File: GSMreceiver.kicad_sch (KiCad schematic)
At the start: 37 parts, among them J1 Conn_01x06_Pin, J2 Conn_02x02_2.54, SW1 SM5-180UP-1, U1 STM32L052C8Tx, Y1 4 MHz, Y2 32768 kHz

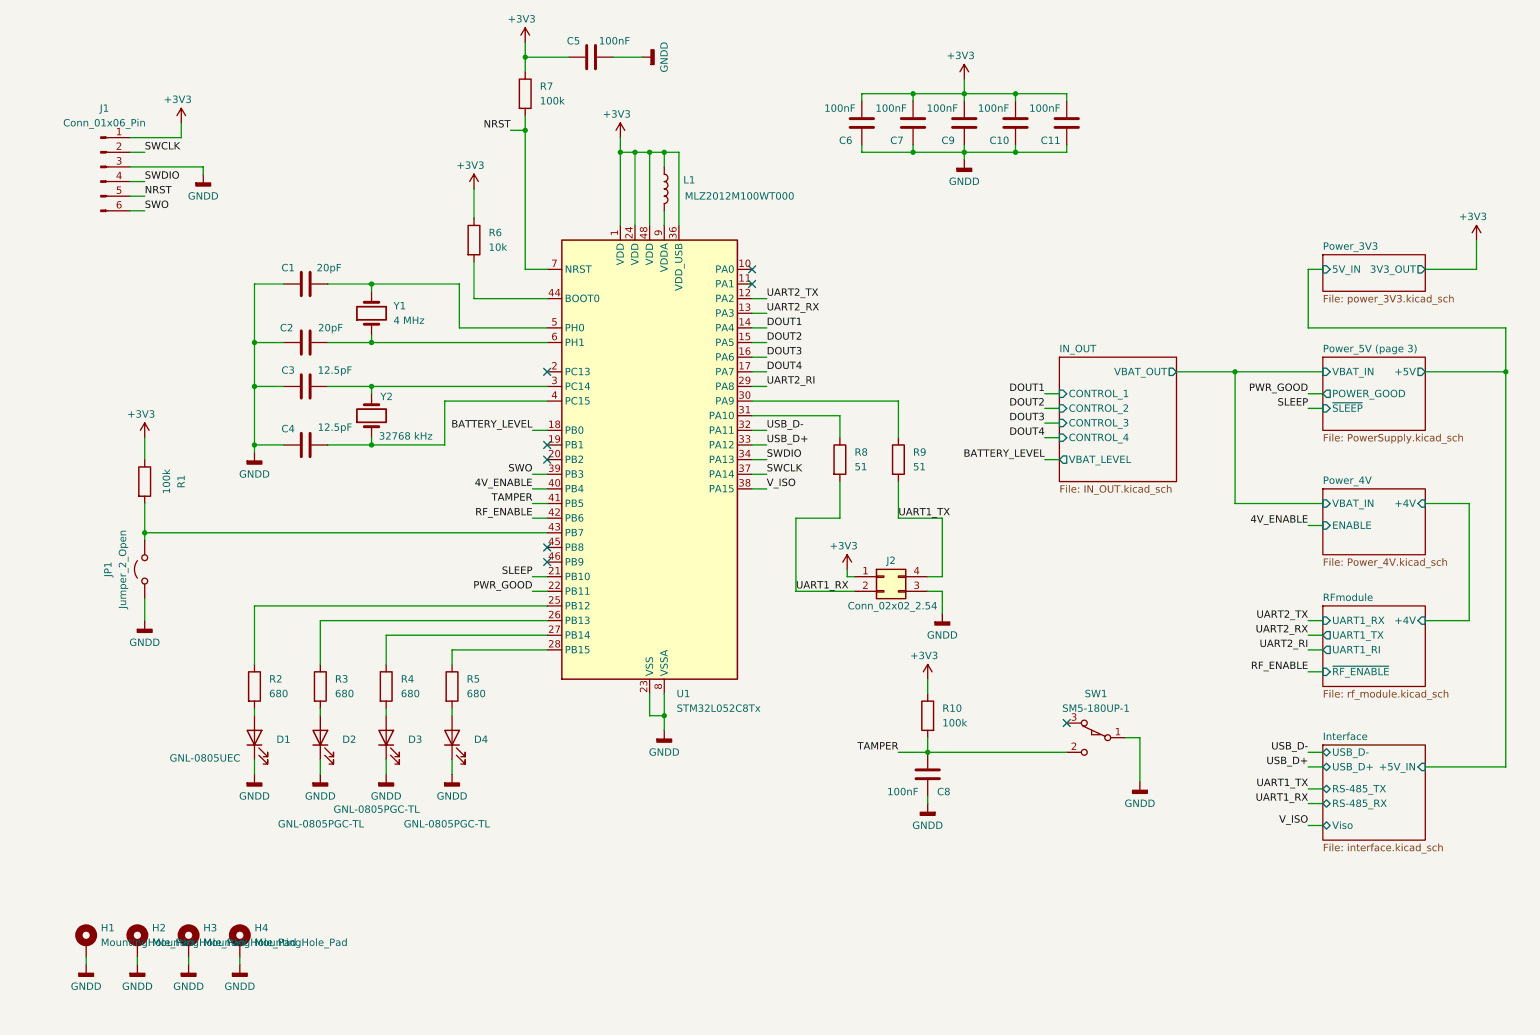
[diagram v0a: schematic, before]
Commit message: Move to SIM800C-DS and two SIM
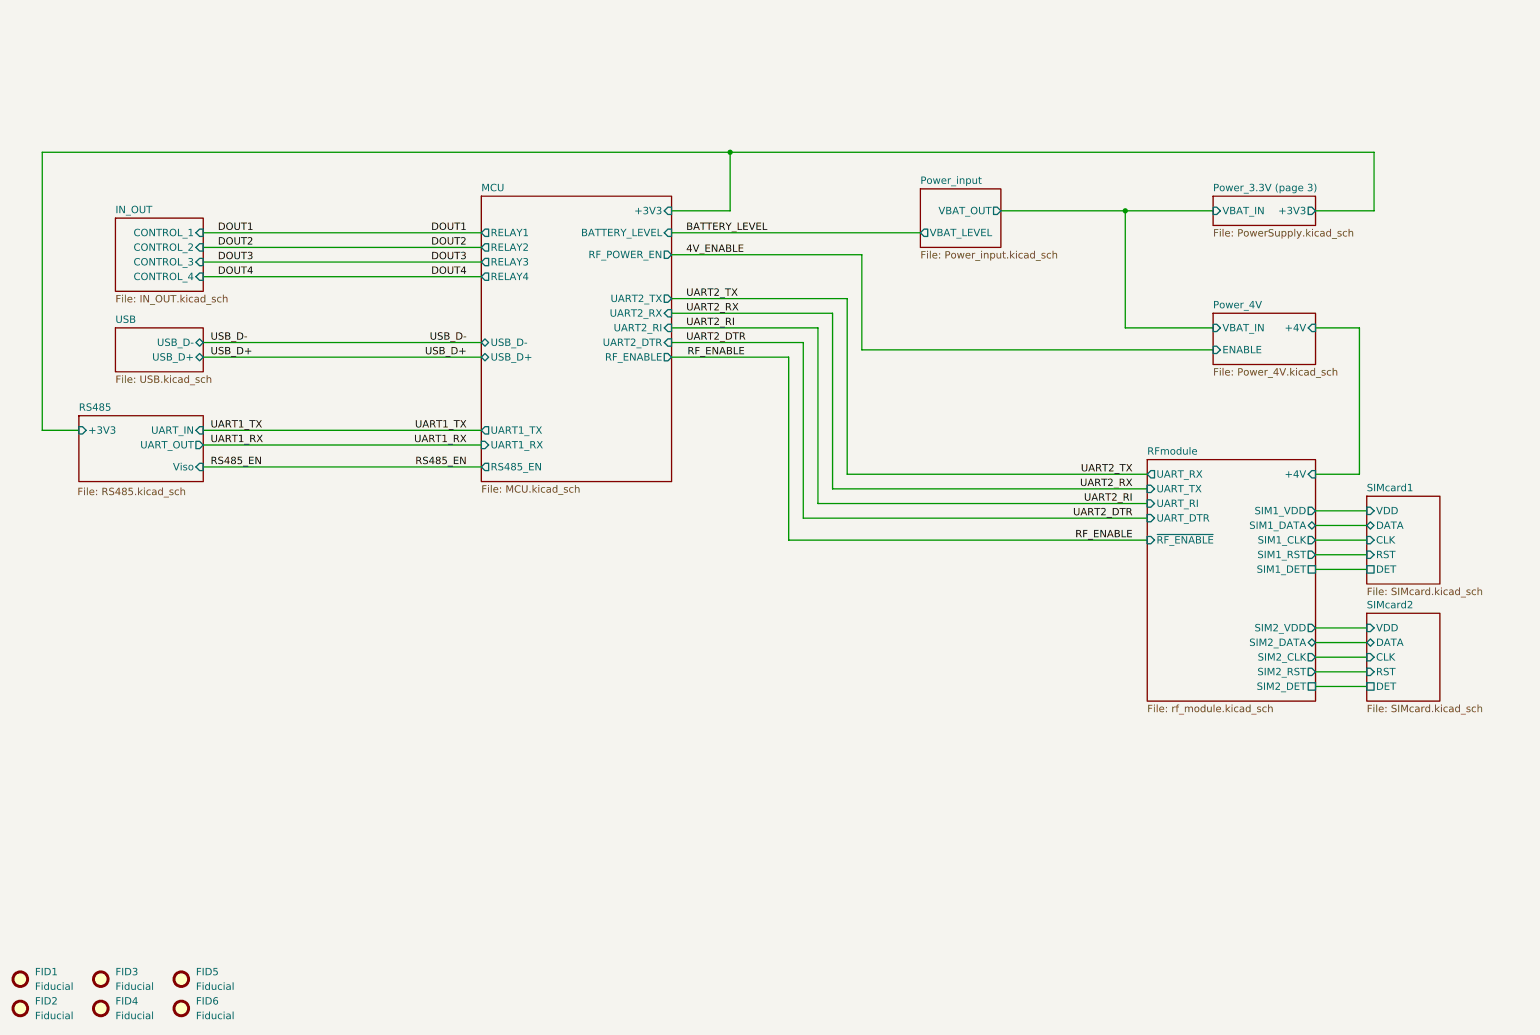
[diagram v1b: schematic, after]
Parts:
- removed C1, C2: 20pF, Capacitor_SMD:C_0805_2012Metric_Pad1.18x1.45mm_HandSolder, symbol Device:C
- removed C10, C11, C5, C6, C7, C8, C9: 100nF, Capacitor_SMD:C_0805_2012Metric_Pad1.18x1.45mm_HandSolder, symbol Device:C
- removed C3, C4: 12.5pF, Capacitor_SMD:C_0805_2012Metric_Pad1.18x1.45mm_HandSolder, symbol Device:C
- removed D1: GNL-0805UEC, LED_SMD:LED_0805_2012Metric_Pad1.15x1.40mm_HandSolder, symbol Device:LED
- removed D2, D3, D4: GNL-0805PGC-TL, LED_SMD:LED_0805_2012Metric_Pad1.15x1.40mm_HandSolder, symbol Device:LED
- removed H1, H2, H3, H4: MountingHole_Pad, MountingHole:MountingHole_4.3mm_M4_DIN965_Pad, symbol Mechanical:MountingHole_Pad
- removed J1: Conn_01x06_Pin, Connector_PinHeader_2.54mm:PinHeader_1x06_P2.54mm_Vertical, symbol Connector:Conn_01x06_Pin
- removed J2: Conn_02x02_2.54, Connector_PinSocket_2.54mm:PinSocket_2x02_P2.54mm_Vertical, symbol Connector_Generic:Conn_02x02_Counter_Clockwise
- removed JP1: Jumper_2_Open, TestPoint:TestPoint_2Pads_Pitch2.54mm_Drill0.8mm, symbol Jumper:Jumper_2_Open
- removed L1: MLZ2012M100WT000, Inductor_SMD:L_0805_2012Metric_Pad1.05x1.20mm_HandSolder, symbol Device:L
- removed R1, R10, R7: 100k, Resistor_SMD:R_0805_2012Metric_Pad1.20x1.40mm_HandSolder, symbol Device:R
- removed R2, R3, R4, R5: 680, Resistor_SMD:R_0805_2012Metric_Pad1.20x1.40mm_HandSolder, symbol Device:R
- removed R6: 10k, Resistor_SMD:R_0805_2012Metric_Pad1.20x1.40mm_HandSolder, symbol Device:R
- removed R8, R9: 51, Resistor_SMD:R_0805_2012Metric_Pad1.20x1.40mm_HandSolder, symbol Device:R
- removed SW1: SM5-180UP-1, footprints:SW_XKB_SM5-180UP-1, symbol symbols:SW_SPDT_XKB_SMx-xxxx-1
- removed U1: STM32L052C8Tx, Package_QFP:LQFP-48_7x7mm_P0.5mm, symbol MCU_ST_STM32L0:STM32L052C8Tx
- removed Y1: 4 MHz, Crystal:Crystal_HC49-4H_Vertical, symbol Device:Crystal
- removed Y2: 32768 kHz, Crystal:Crystal_SMD_EuroQuartz_EQ161-2Pin_3.2x1.5mm_HandSoldering, symbol Device:Crystal
- added FID1, FID2, FID3, FID4, FID5, FID6: Fiducial, Fiducial:Fiducial_1mm_Mask2mm, symbol Mechanical:Fiducial
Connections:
- no-connect marks 8 -> 0
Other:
- sheet Interface renamed USB
- sheet Power_5V (page 3) renamed Power_3.3V (page 3)
- removed sheet Power_3V3
- added sheet MCU (MCU.kicad_sch)
- added sheet Power_input (Power_input.kicad_sch)
- added sheet RS485 (RS485.kicad_sch)
- added sheet SIMcard1 (SIMcard.kicad_sch)
- added sheet SIMcard2 (SIMcard.kicad_sch)
- sheet IN_OUT ports: added none; removed VBAT_LEVEL, VBAT_OUT
- sheet Power_3.3V (page 3) ports: added +3V3; removed +5V, POWER_GOOD, ~{SLEEP}
- sheet RFmodule ports: added SIM1_CLK, SIM1_DATA, SIM1_DET, SIM1_RST, SIM1_VDD, SIM2_CLK, SIM2_DATA, SIM2_DET, SIM2_RST, SIM2_VDD, UART_DTR, UART_RI, UART_RX, UART_TX; removed UART1_RI, UART1_RX, UART1_TX
- sheet USB: file interface.kicad_sch -> USB.kicad_sch
- sheet USB ports: added none; removed +5V_IN, RS-485_RX, RS-485_TX, Viso

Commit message: Proproduction version
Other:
- sheet MCU ports: added VBUS_SENSING; removed none
- sheet USB ports: added VBUS_SENSING; removed none
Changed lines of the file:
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@@
+	(wire
+		(pts
+			(xy 49.53 81.28) (xy 97.79 81.28)
+		)
+		(stroke
+			(width 0)
+			(type default)
+		)
+	)
 	(wire
 		(pts
@@
 		(unit 1)
 		(body_style 1)
-		(exclude_from_sim no)
+		(exclude_from_sim yes)
 		(in_bom no)
 		(on_board yes)
@@
 		(unit 1)
 		(body_style 1)
-		(exclude_from_sim no)
+		(exclude_from_sim yes)
 		(in_bom no)
 		(on_board yes)
@@
 		(unit 1)
 		(body_style 1)
-		(exclude_from_sim no)
+		(exclude_from_sim yes)
 		(in_bom no)
 		(on_board yes)
@@
 		(unit 1)
 		(body_style 1)
-		(exclude_from_sim no)
+		(exclude_from_sim yes)
 		(in_bom no)
 		(on_board yes)
@@
 		(unit 1)
 		(body_style 1)
-		(exclude_from_sim no)
+		(exclude_from_sim yes)
 		(in_bom no)
 		(on_board yes)
@@
 		(unit 1)
 		(body_style 1)
-		(exclude_from_sim no)
+		(exclude_from_sim yes)
 		(in_bom no)
 		(on_board yes)
@@
 			)
 		)
+		(pin "VBUS_SENSING" input
+			(at 97.79 81.28 180)
+			(effects
+				(font
+					(size 1.27 1.27)
+				)
+				(justify left)
+			)
+		)
 		(instances
 			(project "GSMreceiver"
@@
 	)
 	(sheet
-		(at 34.29 73.66)
-		(size 15.24 7.62)
+		(at 33.02 73.66)
+		(size 16.51 10.16)
 		(exclude_from_sim no)
 		(in_bom yes)
@@
 		)
 		(property "Sheetname" "USB"
-			(at 34.29 72.9484 0)
+			(at 33.02 72.9484 0)
 			(show_name no)
 			(do_not_autoplace no)
@@
 		)
 		(property "Sheetfile" "USB.kicad_sch"
-			(at 34.29 81.8646 0)
+			(at 33.02 84.4046 0)
 			(show_name no)
 			(do_not_autoplace no)
@@
 			(effects
 				(font
+					(size 1.27 1.27)
+				)
+				(justify right)
+			)
+		)
+		(pin "VBUS_SENSING" output
+			(at 49.53 81.28 0)
+			(effects
+				(font
